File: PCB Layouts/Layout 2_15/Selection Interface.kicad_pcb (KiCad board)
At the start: 4 copper layers, 110 x 90 mm, 132 parts, among them P1 CONN_01X02, P11 CONN_01X02, P12 CONN_01X02, P13 CONN_01X10, P14 CONN_01X02, P15 CONN_01X02, P16 CONN_01X02, P18 CONN_02X05, P2 CONN_01X02, P3 CONN_01X02, P4 CONN_01X02, P5 CONN_01X02, P6 CONN_02X10, P7 CONN_01X02, P8 CONN_02X04, P9 CONN_01X02

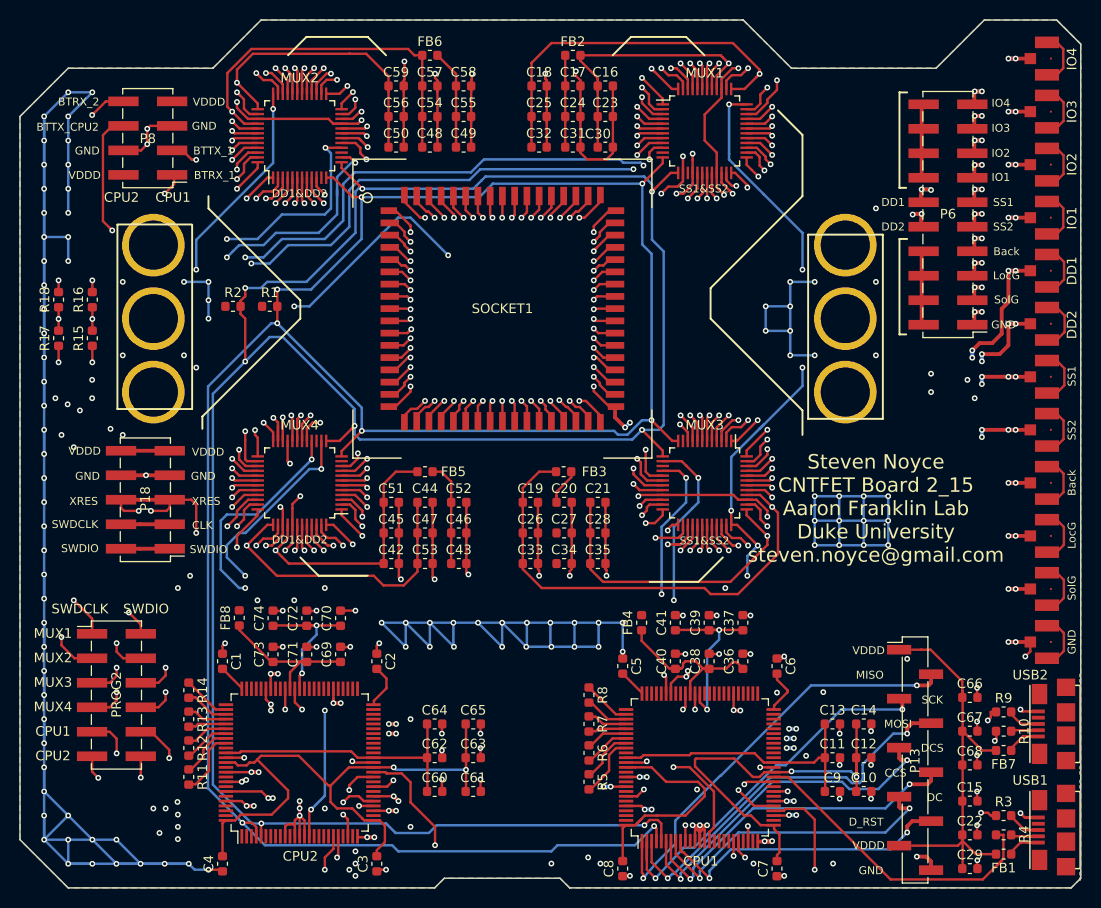
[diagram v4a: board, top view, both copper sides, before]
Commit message: Updated PCB schematic to use more standardized symbols and only symbols from a single custom schematic library (in the "lib" sub-folder). Trying to remove excess, irrelevant files that have been auto-generated over many design iterations
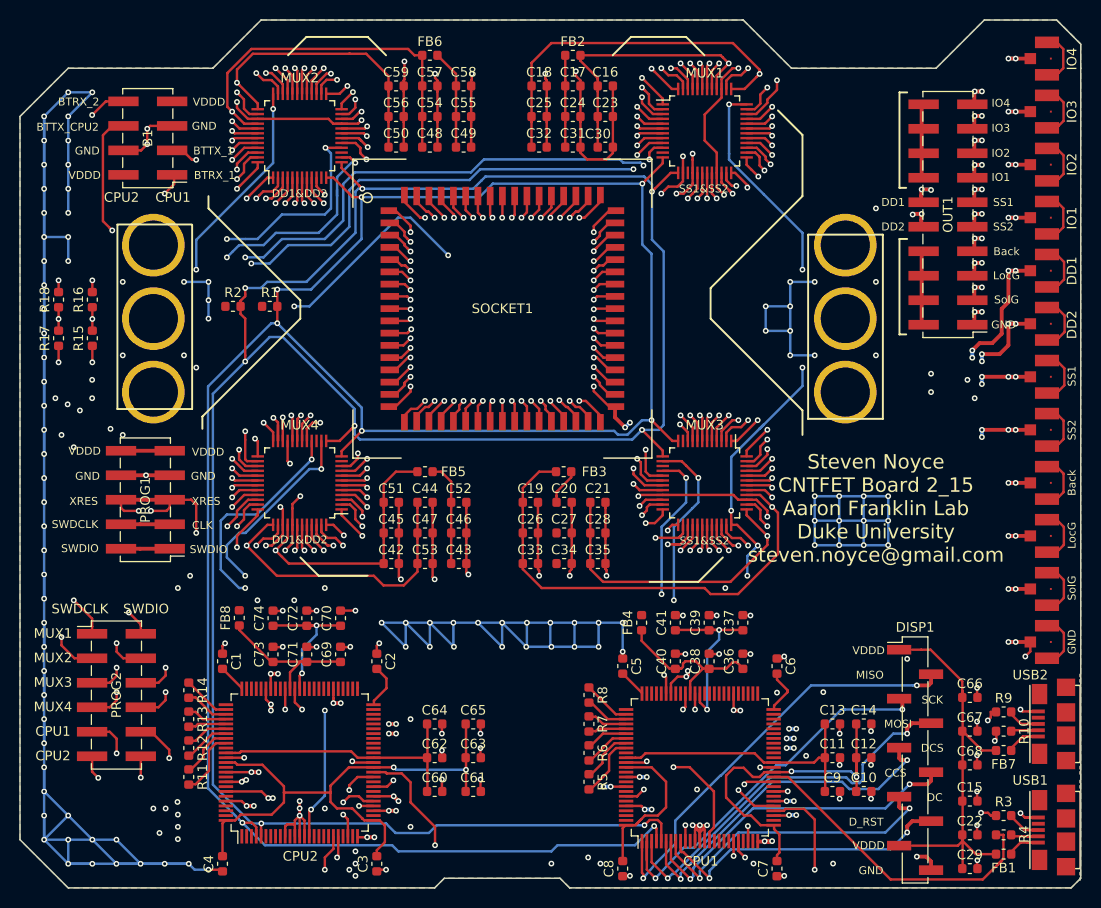
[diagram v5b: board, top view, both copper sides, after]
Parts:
- removed P13: CONN_01X10, Connector_PinHeader_2.54mm:PinHeader_1x10_P2.54mm_Vertical_SMD_Pin1Left
- removed P18: CONN_02X05, Connector_PinHeader_2.54mm:PinHeader_2x05_P2.54mm_Vertical_SMD
- removed P6: CONN_02X10, Connector_PinHeader_2.54mm:PinHeader_2x10_P2.54mm_Vertical_SMD
- removed P8: CONN_02X04, Connector_PinHeader_2.54mm:PinHeader_2x04_P2.54mm_Vertical_SMD
- added B1: Conn_02x04_Odd_Even, Connector_PinHeader_2.54mm:PinHeader_2x04_P2.54mm_Vertical_SMD, F.Cu at (163.2, 82.2)
- added DISP1: Conn_01x10, Connector_PinHeader_2.54mm:PinHeader_1x10_P2.54mm_Vertical_SMD_Pin1Left, F.Cu at (242.8, 146.7)
- added OUT1: Conn_02x10_Odd_Even, Connector_PinHeader_2.54mm:PinHeader_2x10_P2.54mm_Vertical_SMD, F.Cu at (246.2, 90.2)
- added PROG1: Conn_02x05_Odd_Even, Connector_PinHeader_2.54mm:PinHeader_2x05_P2.54mm_Vertical_SMD, F.Cu at (163.0, 119.8)
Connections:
- net Net-(C11-Pad1) renamed VCCD_C1
- net Net-(C16-Pad1) renamed VDDA_M1
- net Net-(C18-Pad1) renamed VCCD_M1
- net Net-(C19-Pad1) renamed VDDA_M3
- net Net-(C21-Pad1) renamed VCCD_M3
- net Net-(C36-Pad1) renamed VDDA_C1
- net Net-(C37-Pad1) renamed VCCA_C1
- net Net-(C42-Pad1) renamed VDDA_M4
- net Net-(C44-Pad1) renamed VCCD_M4
- net Net-(C48-Pad1) renamed VDDA_M2
- net Net-(C50-Pad1) renamed VCCD_M2
- net Net-(C60-Pad1) renamed VCCD_C2
- net Net-(C69-Pad1) renamed VDDA_C2
- net Net-(C70-Pad1) renamed VCCA_C2
- net Net-(CPU1-Pad35) renamed USBDP_C1
- net Net-(CPU1-Pad36) renamed USBDM_C1
- net Net-(CPU2-Pad35) renamed USBDP_C2
- net Net-(CPU2-Pad36) renamed USBDM_C2
- net Net-(FB1-Pad1) renamed VBUS1
- net Net-(FB7-Pad1) renamed VBUS2
- net Net-(P8-Pad1) renamed BT1_RXR
- net Net-(P8-Pad8) renamed BT2_RXR
- net Net-(R10-Pad2) renamed USB2_D-
- net Net-(R3-Pad2) renamed USB1_D+
- net Net-(R4-Pad2) renamed USB1_D-
- net Net-(R9-Pad2) renamed USB2_D+
- net Net-(USB1-Pad4) renamed USB1_ID
- net Net-(USB2-Pad4) renamed USB2_ID
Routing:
- net VDDD: track 300.1 -> 281.8 mm
- net Net-(P6-Pad2): track 7.62 -> 0.00 mm
- net Net-(OUT1-Pad2): track 0.00 -> 7.62 mm
- net Net-(P6-Pad14): track 7.62 -> 0.00 mm
- net Net-(OUT1-Pad14): track 0.00 -> 7.62 mm

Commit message: Finished converting all connector components to the standard library in layout 2_15
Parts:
- removed P1, P11, P12, P14, P15, P16, P2, P3, P4, P5, P7, P9: CONN_01X02, Custom_Footprint_Library:IPEX_Connector_SMD_(RECE.20279.001E.01)
- added IPEX1: Conn_01x02, Custom_Footprint_Library:IPEX_Connector_SMD_(RECE.20279.001E.01), F.Cu at (255.2, 134.5)
- added IPEX10: Conn_01x02, Custom_Footprint_Library:IPEX_Connector_SMD_(RECE.20279.001E.01), F.Cu at (255.2, 85.0)
- added IPEX11: Conn_01x02, Custom_Footprint_Library:IPEX_Connector_SMD_(RECE.20279.001E.01), F.Cu at (255.2, 79.5)
- added IPEX12: Conn_01x02, Custom_Footprint_Library:IPEX_Connector_SMD_(RECE.20279.001E.01), F.Cu at (255.2, 74.0)
- added IPEX2: Conn_01x02, Custom_Footprint_Library:IPEX_Connector_SMD_(RECE.20279.001E.01), F.Cu at (255.2, 129.0)
- added IPEX3: Conn_01x02, Custom_Footprint_Library:IPEX_Connector_SMD_(RECE.20279.001E.01), F.Cu at (255.2, 123.5)
- added IPEX4: Conn_01x02, Custom_Footprint_Library:IPEX_Connector_SMD_(RECE.20279.001E.01), F.Cu at (255.2, 118.0)
- added IPEX5: Conn_01x02, Custom_Footprint_Library:IPEX_Connector_SMD_(RECE.20279.001E.01), F.Cu at (255.2, 112.5)
- added IPEX6: Conn_01x02, Custom_Footprint_Library:IPEX_Connector_SMD_(RECE.20279.001E.01), F.Cu at (255.2, 107.0)
- added IPEX7: Conn_01x02, Custom_Footprint_Library:IPEX_Connector_SMD_(RECE.20279.001E.01), F.Cu at (255.2, 101.5)
- added IPEX8: Conn_01x02, Custom_Footprint_Library:IPEX_Connector_SMD_(RECE.20279.001E.01), F.Cu at (255.2, 96.0)
- added IPEX9: Conn_01x02, Custom_Footprint_Library:IPEX_Connector_SMD_(RECE.20279.001E.01), F.Cu at (255.2, 90.5)
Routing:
- net Net-(P9-Pad2): track 6.88 -> 0.00 mm
- net Net-(IPEX7-Pad2): track 0.00 -> 6.88 mm
- net Net-(P7-Pad2): track 6.86 -> 0.00 mm
- net Net-(IPEX6-Pad2): track 0.00 -> 6.86 mm
- net Net-(P11-Pad2): track 6.83 -> 0.00 mm
- net Net-(IPEX8-Pad2): track 0.00 -> 6.83 mm
- net Net-(P3-Pad2): track 6.81 -> 0.00 mm
- net Net-(P2-Pad2): track 6.81 -> 0.00 mm
- net Net-(IPEX3-Pad2): track 0.00 -> 6.81 mm
- net Net-(IPEX2-Pad2): track 0.00 -> 6.81 mm
- net Net-(P5-Pad2): track 6.79 -> 0.00 mm
- net Net-(IPEX5-Pad2): track 0.00 -> 6.79 mm
- net Net-(P15-Pad2): track 6.79 -> 0.00 mm
- net Net-(IPEX11-Pad2): track 0.00 -> 6.79 mm
- net Net-(P14-Pad2): track 6.79 -> 0.00 mm
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
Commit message: A few more updates to PCB layout
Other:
- board text added: "BackG"

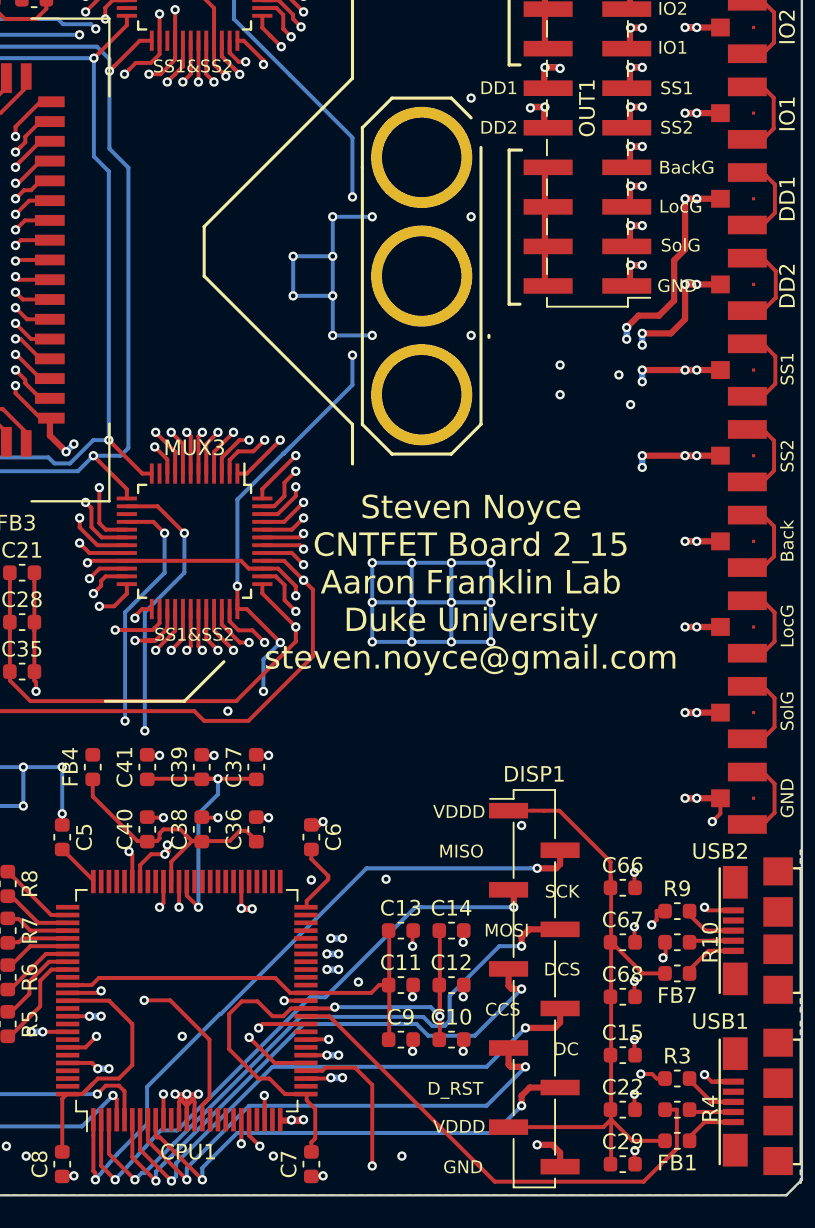
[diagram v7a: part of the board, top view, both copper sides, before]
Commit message: Physically interrupted all three gate pins so that they are not permanently tied to the PSoC. This means you could supply an external power supply (or boost converter, etc) that would apply larger gate voltages to the chip in the socket.
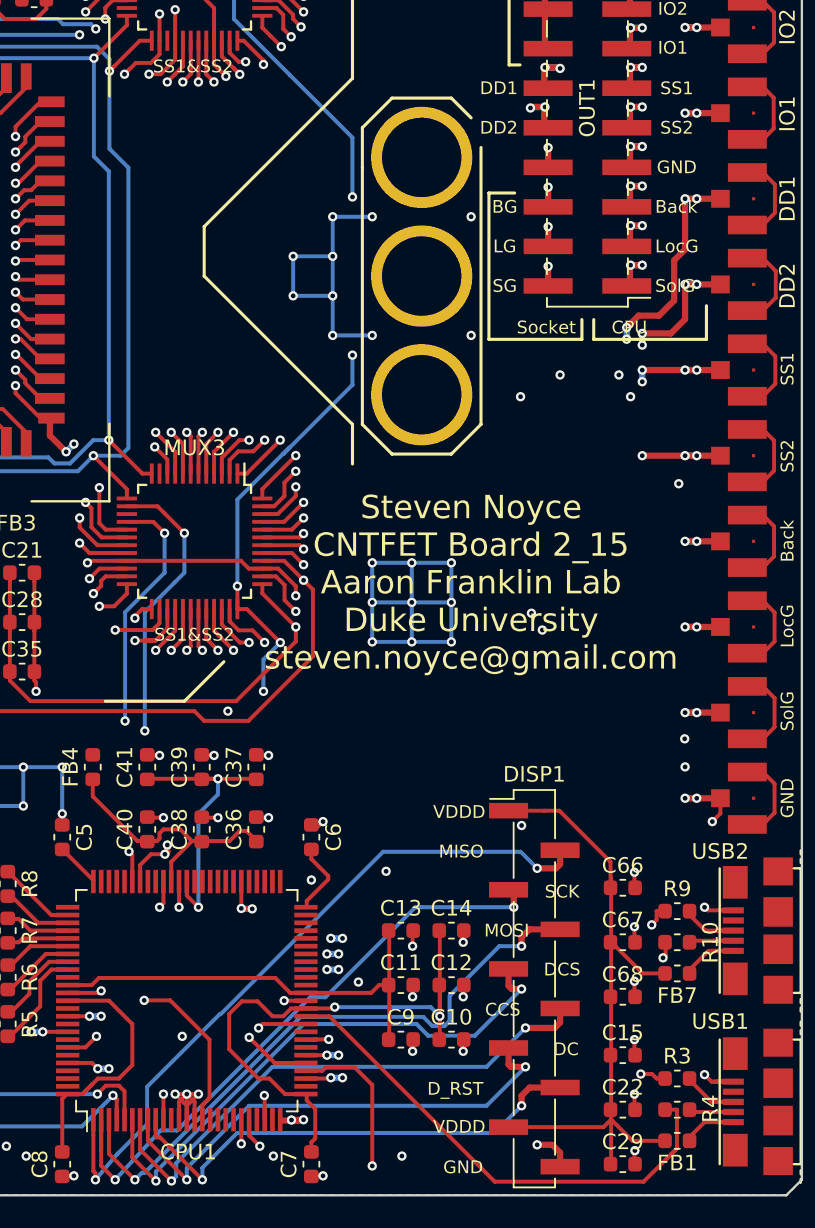
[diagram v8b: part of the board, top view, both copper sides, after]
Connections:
- IPEX2 pad 1: SolutionGate -> SolutionGate_Socket
- IPEX3 pad 1: LocalGates -> LocalGates_Socket
- IPEX4 pad 1: BackGate -> BackGate_Socket
- OUT1 pad 1: GND -> SolutionGate
- OUT1 pad 2: Net-(OUT1-Pad2) -> SolutionGate_Socket
- OUT1 pad 3: SolutionGate -> LocalGates
- OUT1 pad 4: Net-(OUT1-Pad2) -> LocalGates_Socket
- OUT1 pad 5: LocalGates -> BackGate
- OUT1 pad 6: Net-(OUT1-Pad2) -> BackGate_Socket
- OUT1 pad 7: BackGate -> GND
- OUT1 pad 8: Net-(OUT1-Pad2) -> GND
- SOCKET1 pad 33: LocalGates -> LocalGates_Socket
- SOCKET1 pad 34: SolutionGate -> SolutionGate_Socket
- SOCKET1 pad 68: BackGate -> BackGate_Socket
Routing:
- net SolutionGate_Socket: track 0.00 -> 94.1 mm, vias 0 -> 5
- net LocalGates_Socket: track 0.00 -> 91.4 mm, vias 0 -> 5
- net BackGate_Socket: track 0.00 -> 79.7 mm, vias 0 -> 6
- net SolutionGate: track 181.1 -> 116.8 mm, vias 9 -> 6
- net LocalGates: track 177.1 -> 116.6 mm, vias 9 -> 7
- net BackGate: track 173.4 -> 119.5 mm, vias 11 -> 8
- net GND: track 609.2 -> 597.7 mm, vias 192 -> 189
- net Net-(OUT1-Pad2): track 7.62 -> 0.00 mm
- net DD2: track 282.5 -> 285.2 mm
- net DisplayMISO: track 44.5 -> 45.4 mm
- net SS2: track 202.0 -> 201.7 mm, vias 13 -> 12
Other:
- board text added: "BG"
- board text added: "CPU"
- board text added: "LG"
- board text added: "SG"
- board text added: "Socket"
- board text removed: "BackG"
